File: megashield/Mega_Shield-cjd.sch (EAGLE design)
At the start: 17 parts

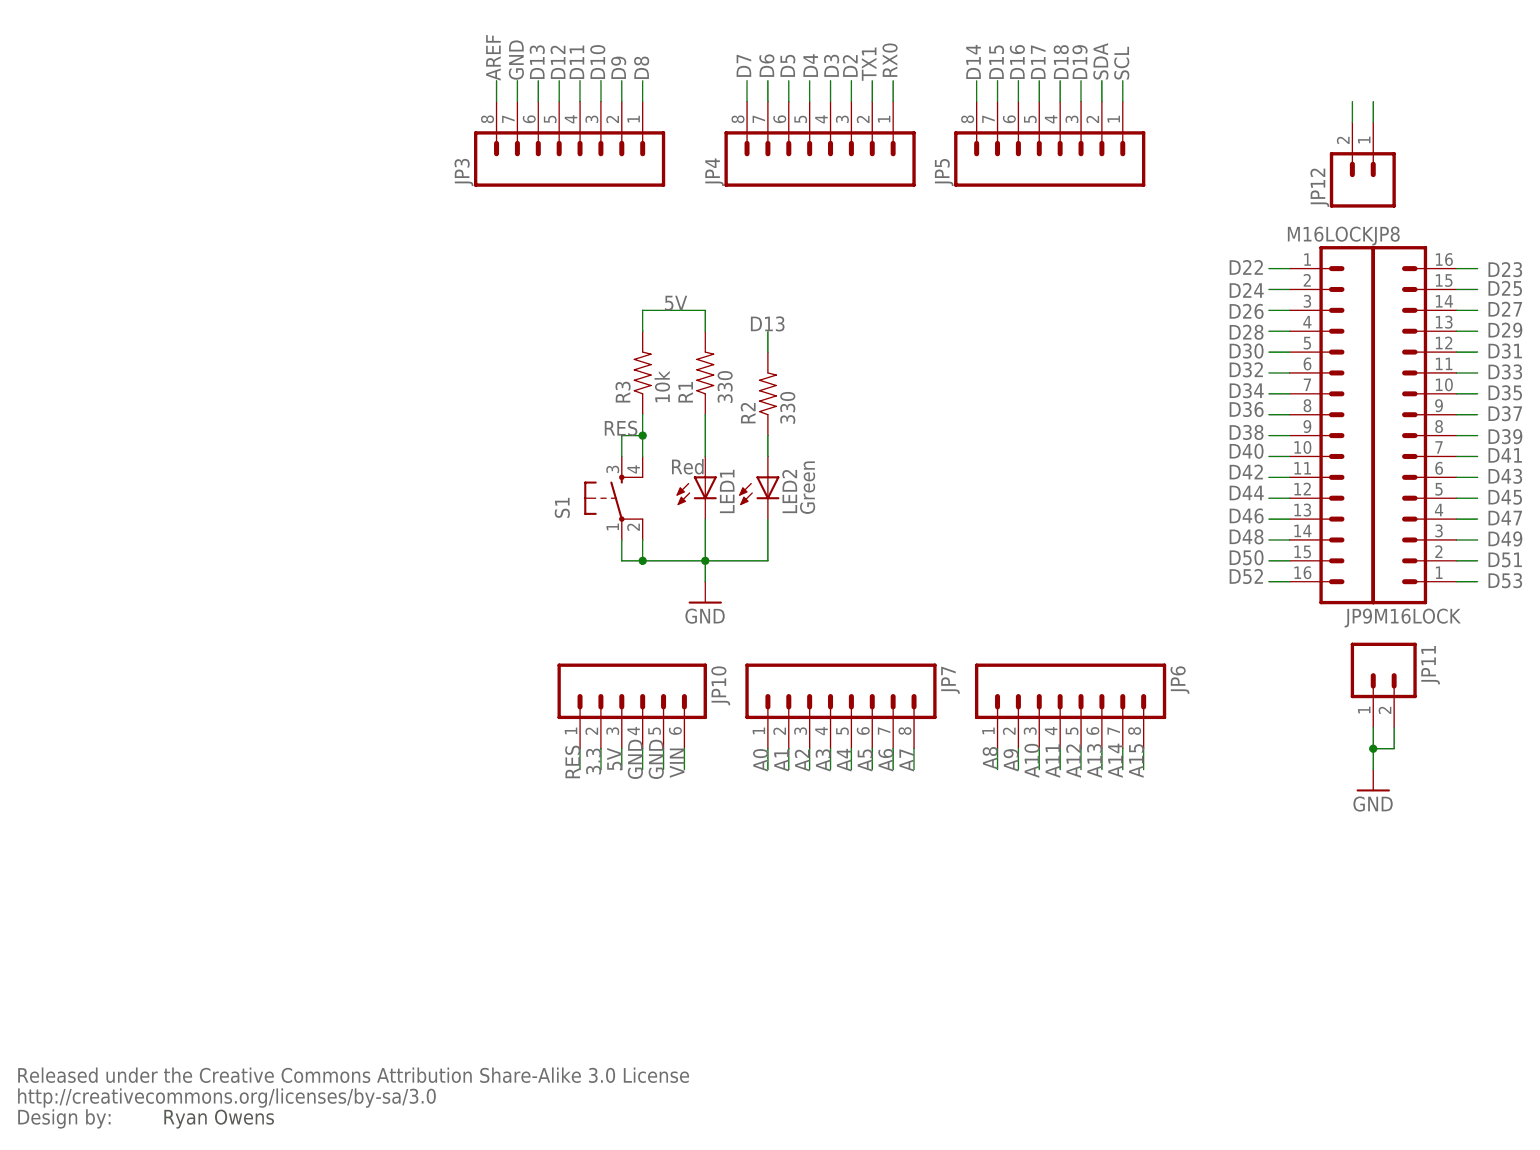
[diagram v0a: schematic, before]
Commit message: Update with larger busses
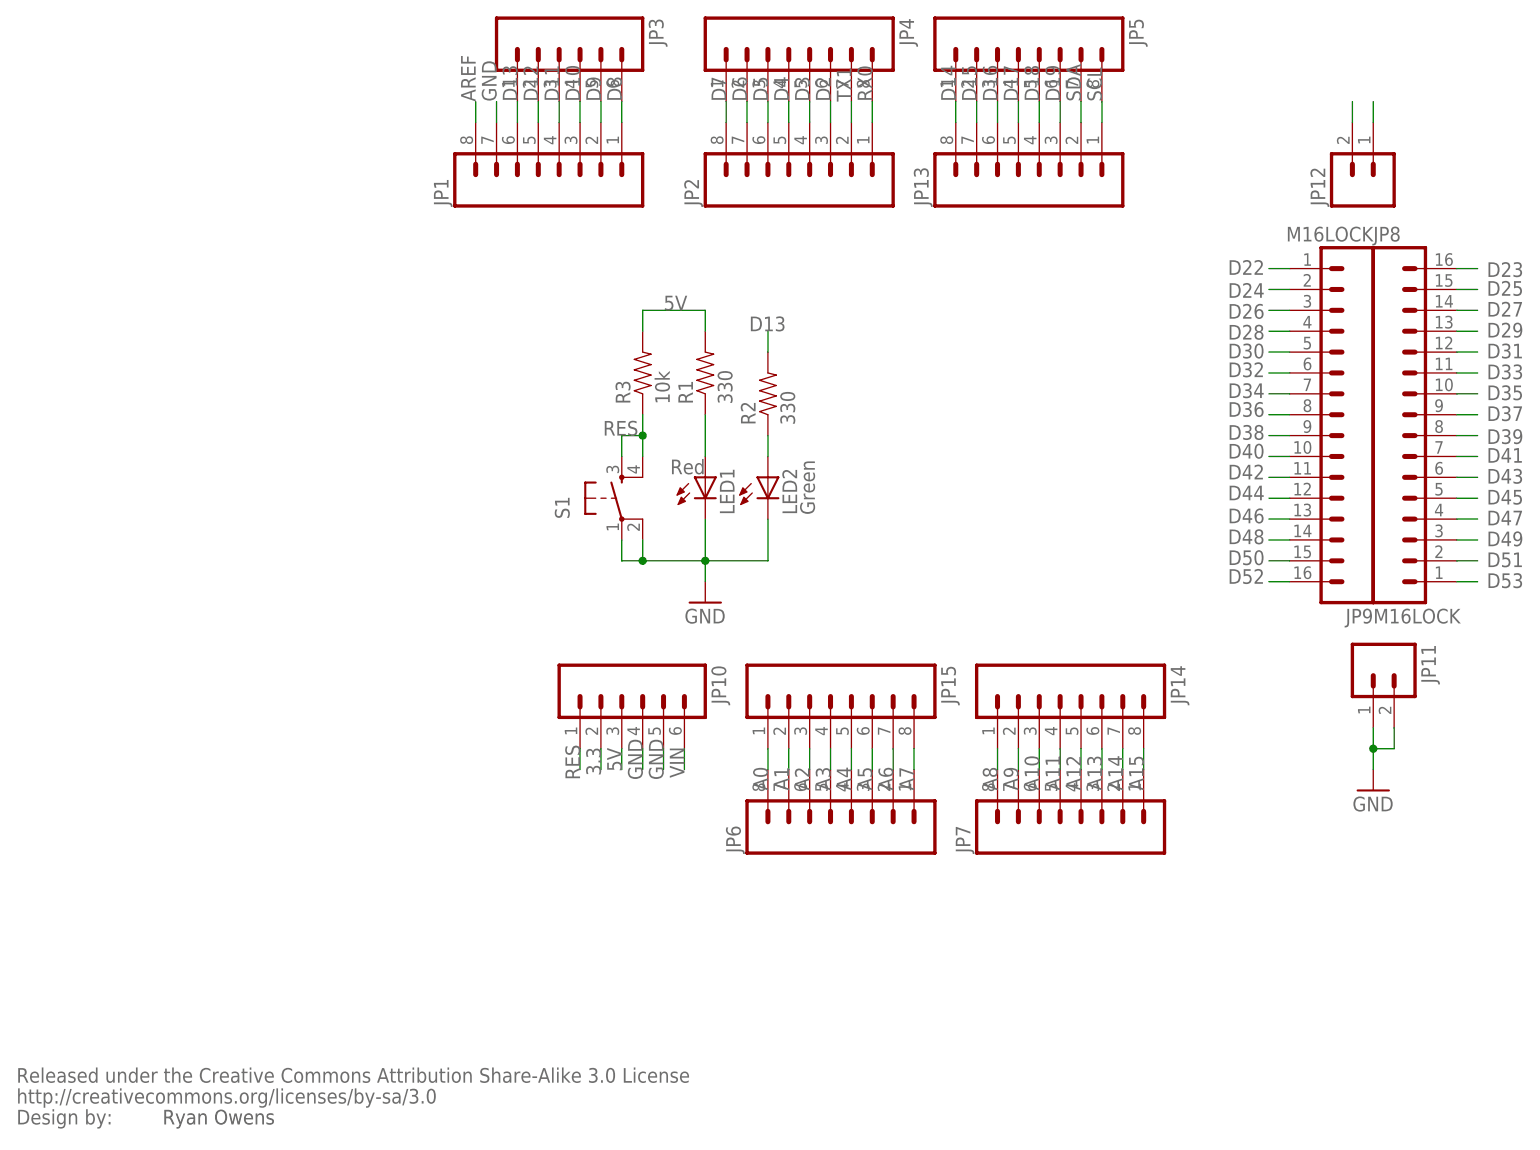
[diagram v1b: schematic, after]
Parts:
- added JP1, JP13, JP14, JP15, JP2: (no value), SparkFun-Connectors:M081X08_LOCK_NO_PIN1
- JP3: device SparkFun:M08LOCK -> SparkFun-Connectors:M06NO_SILK_FEMALE_PTH
- JP4, JP5, JP6, JP7: device SparkFun:M08LOCK -> SparkFun-Connectors:M08NO_SILK_FEMALE_PTH
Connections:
- net A0: now also JP15.1, JP6.8; no longer JP7.1
- net A1: now also JP15.2, JP6.7; no longer JP7.2
- net A10: now also JP14.3, JP7.6; no longer JP6.3
- net A11: now also JP14.4, JP7.5; no longer JP6.4
- net A12: now also JP14.5, JP7.4; no longer JP6.5
- net A13: now also JP14.6, JP7.3; no longer JP6.6
- net A14: now also JP14.7, JP7.2; no longer JP6.7
- net A15: now also JP14.8, JP7.1; no longer JP6.8
- net A2: now also JP15.3, JP6.6; no longer JP7.3
- net A3: now also JP15.4, JP6.5; no longer JP7.4
- net A4: now also JP15.5, JP6.4; no longer JP7.5
- net A5: now also JP15.6, JP6.3; no longer JP7.6
- net A6: now also JP15.7, JP6.2; no longer JP7.7
- net A7: now also JP15.8, JP6.1; no longer JP7.8
- net A8: now also JP14.1, JP7.8; no longer JP6.1
- net A9: now also JP14.2, JP7.7; no longer JP6.2
- net AREF: now also JP1.8; no longer JP3.8
- net D10: now also JP1.3, JP3.4; no longer JP3.3
- net D11: now also JP1.4, JP3.3; no longer JP3.4
- net D12: now also JP1.5, JP3.2; no longer JP3.5
- net D13: now also JP1.6, JP3.1; no longer JP3.6
- net D14: now also JP13.8, JP5.1; no longer JP5.8
- net D15: now also JP13.7, JP5.2; no longer JP5.7
- net D16: now also JP13.6, JP5.3; no longer JP5.6
- net D17: now also JP13.5, JP5.4; no longer JP5.5
- net D18: now also JP13.4, JP5.5; no longer JP5.4
- net D19: now also JP13.3, JP5.6; no longer JP5.3
- net D2: now also JP2.3, JP4.6; no longer JP4.3
- net D3: now also JP2.4, JP4.5; no longer JP4.4
- net D4: now also JP2.5, JP4.4; no longer JP4.5
- net D5: now also JP2.6, JP4.3; no longer JP4.6
- net D6: now also JP2.7, JP4.2; no longer JP4.7
- net D7: now also JP2.8, JP4.1; no longer JP4.8
- net D8: now also JP1.1, JP3.6; no longer JP3.1
- net D9: now also JP1.2, JP3.5; no longer JP3.2
- net GND: now also JP1.7; no longer JP3.7
- net RX0: now also JP2.1, JP4.8; no longer JP4.1
- net SCL: now also JP13.1, JP5.8; no longer JP5.1
- net SDA: now also JP13.2, JP5.7; no longer JP5.2
- net TX1: now also JP2.2, JP4.7; no longer JP4.2
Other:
- moved on the sheet: JP4, JP5, JP6, JP7
